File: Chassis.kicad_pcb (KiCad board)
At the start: 2 copper layers, 10 parts, among them J1 Conn_01x02, J10 Conn_01x02, J2 Conn_01x02, J3 Conn_01x02, J4 Conn_01x02, J5 Conn_01x02, J6 Conn_01x02, J7 Conn_01x02, J8 Conn_01x02, J9 Conn_01x02

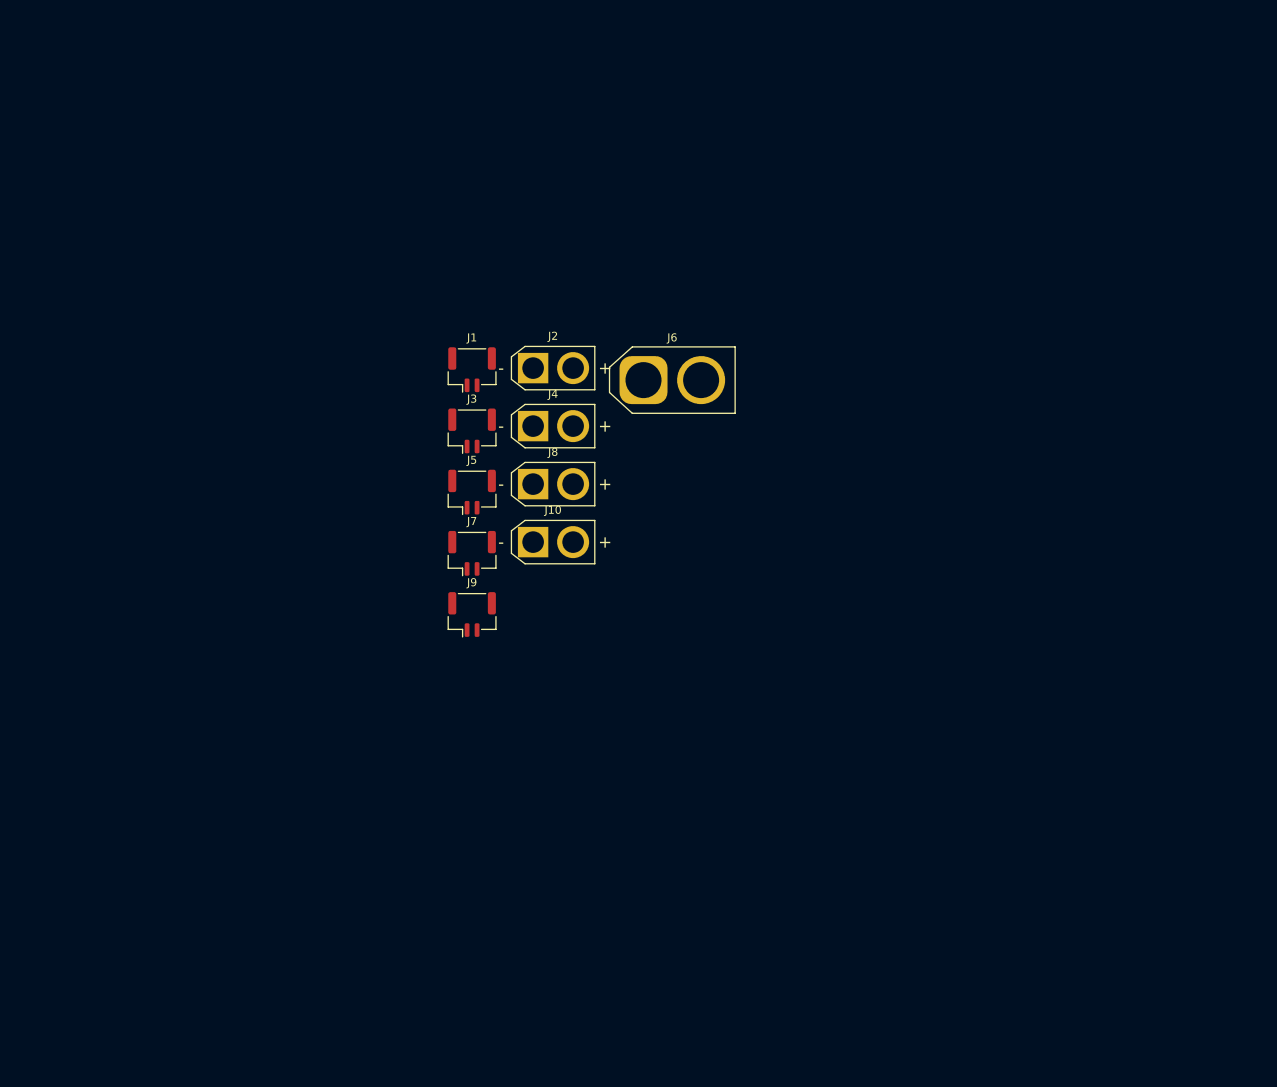
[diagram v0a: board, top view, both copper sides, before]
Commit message: Change polarity of pins + add circular trace
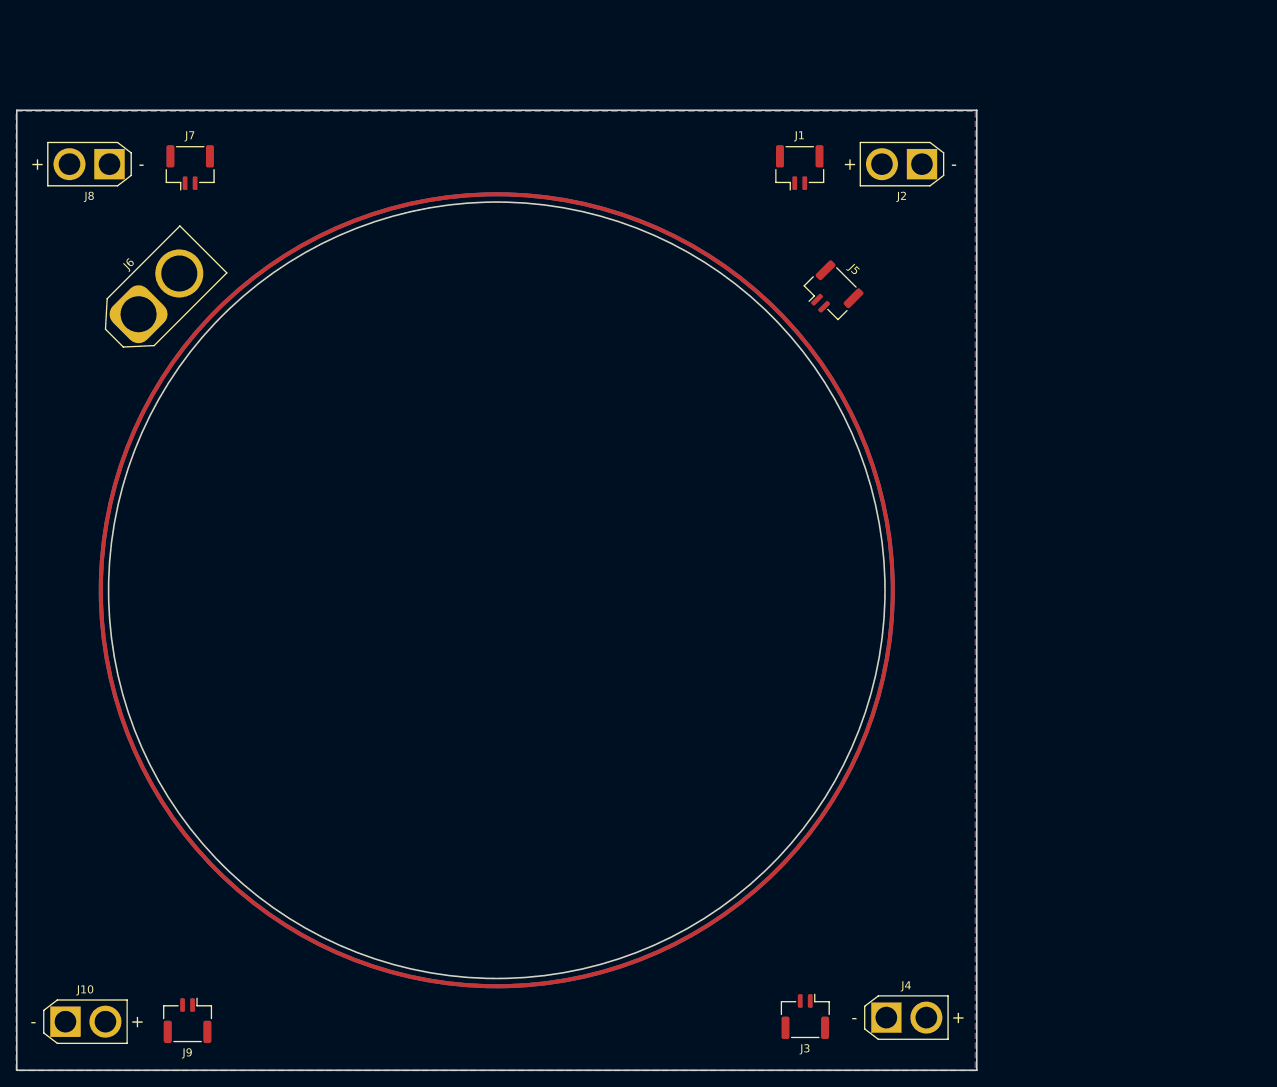
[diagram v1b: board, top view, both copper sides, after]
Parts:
- moved J4 86.1 mm to (168.7, 153.4)
- moved J3 84.2 mm to (158.6, 153.3), turned to 180 degrees
- moved J10 83.7 mm to (66.1, 153.9)
- moved J8 66.4 mm to (71.6, 46.7), turned to 180 degrees
- moved J6 63.7 mm to (75.2, 65.5), turned to 45 degrees
- moved J9 62.0 mm to (81.3, 153.8), turned to 180 degrees
- moved J7 59.7 mm to (81.7, 47.2)
- moved J2 54.9 mm to (173.1, 46.7), turned to 180 degrees
- moved J5 51.4 mm to (161.9, 62.7), turned to -45 degrees
- moved J1 48.1 mm to (157.9, 47.2)
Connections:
- J1 pad 1: /CAN+ -> /CAN-
- J1 pad 2: /CAN- -> /CAN+
- J10 pad 1: /VIN -> /GND
- J10 pad 2: /GND -> /VIN
- J2 pad 1: /VIN -> /GND
- J2 pad 2: /GND -> /VIN
- J3 pad 1: /CAN+ -> /CAN-
- J3 pad 2: /CAN- -> /CAN+
- J4 pad 1: /VIN -> /GND
- J4 pad 2: /GND -> /VIN
- J5 pad 1: /CAN+ -> /CAN-
- J5 pad 2: /CAN- -> /CAN+
- J6 pad 1: /VIN -> /GND
- J6 pad 2: /GND -> /VIN
- J7 pad 1: /CAN+ -> /CAN-
- J7 pad 2: /CAN- -> /CAN+
- J8 pad 1: /VIN -> /GND
- J8 pad 2: /GND -> /VIN
- J9 pad 1: /CAN+ -> /CAN-
- J9 pad 2: /CAN- -> /CAN+
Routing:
- added copper zone on B.Cu, net /GND
- added copper zone on F.Cu, net /VIN
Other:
- board outline added: 120 x 120 mm

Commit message: Routed CAN lines + made hole octagonal
+ differential pair skew fixed
Dimensions may be subject to change, will have to redimension and reroute
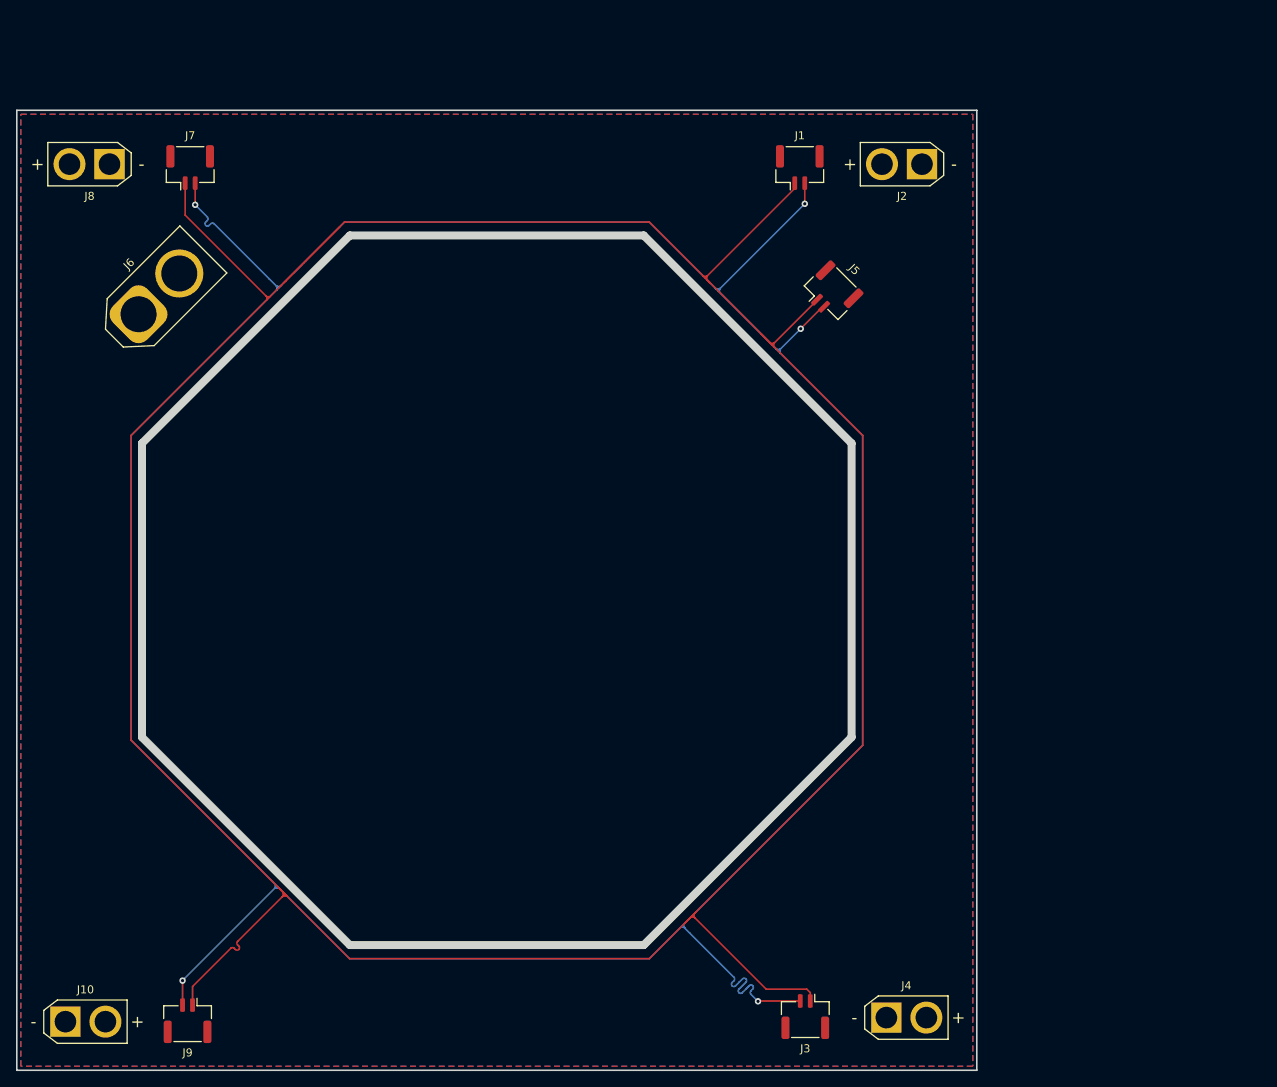
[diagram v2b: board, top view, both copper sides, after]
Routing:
- net /CAN+: track 0.00 -> 417.9 mm, vias 0 -> 5
- net /CAN-: track 0.00 -> 407.2 mm
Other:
- outline, holes or cut-outs redrawn

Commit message: Fixed colinear traces
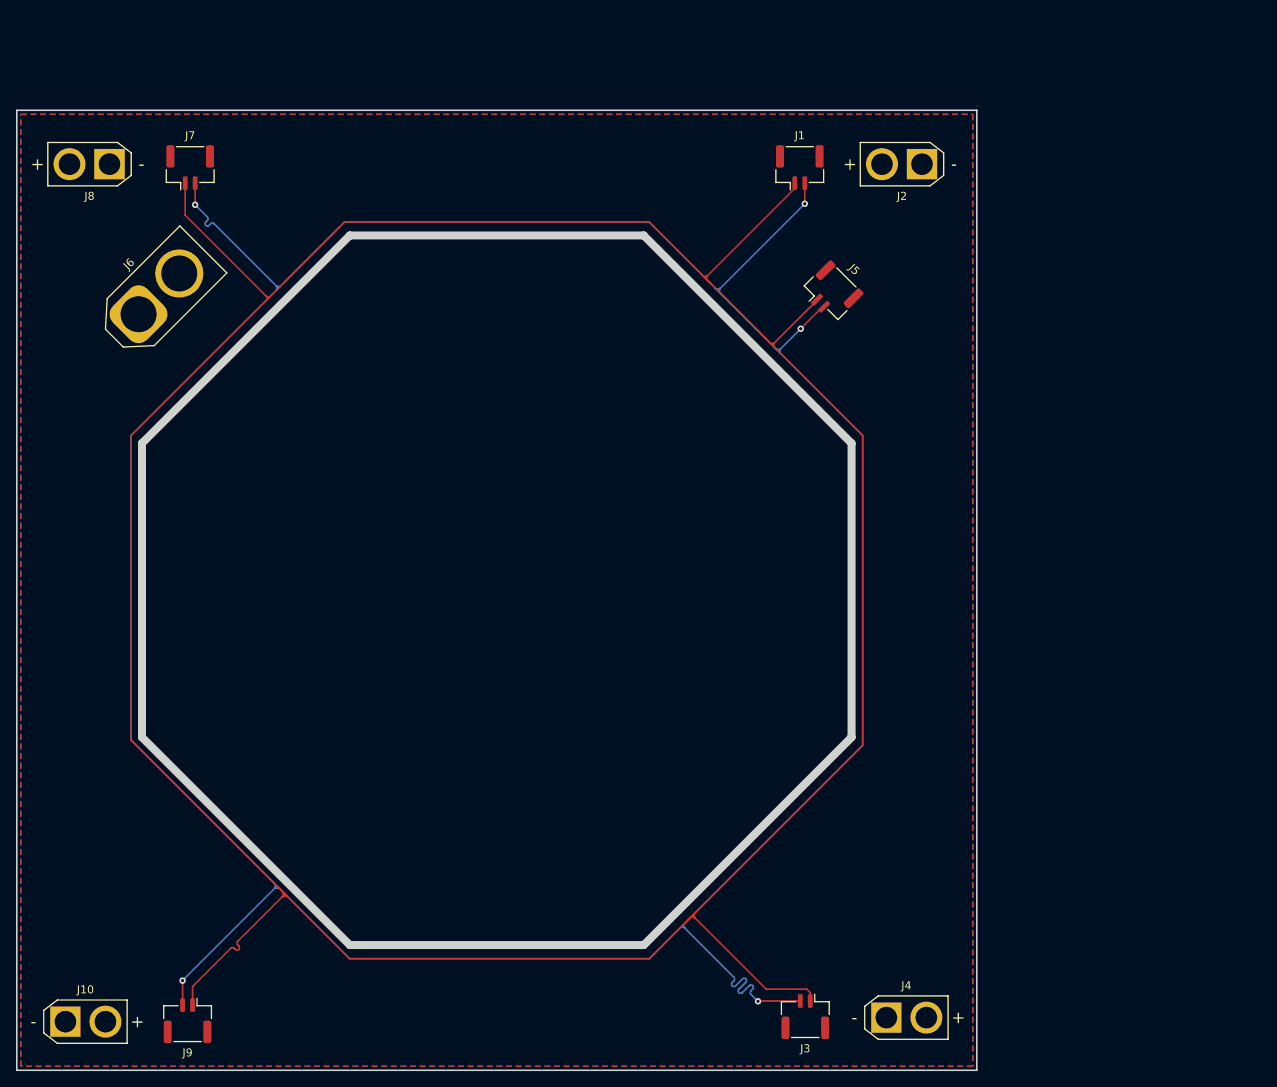
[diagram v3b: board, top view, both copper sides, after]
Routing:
- net /CAN+: track 417.9 -> 416.3 mm
- net /CAN-: track 407.2 -> 406.5 mm

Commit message: Completed initial layout
I'm going to get roasted over some of these choices
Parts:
- added C1: 4.7µF, Capacitor_SMD:C_0603_1608Metric_Pad1.08x0.95mm_HandSolder, F.Cu at (176.2, 145.1)
- added C2: 4.7µF, Capacitor_SMD:C_0603_1608Metric_Pad1.08x0.95mm_HandSolder, F.Cu at (176.2, 147.6)
- added C3: 10nF, Capacitor_SMD:C_0603_1608Metric_Pad1.08x0.95mm_HandSolder, F.Cu at (161.5, 141.7)
- added C4: 22µF, Capacitor_SMD:C_0805_2012Metric_Pad1.18x1.45mm_HandSolder, F.Cu at (176.5, 131.6)
- added C5: 22µF, Capacitor_SMD:C_0805_2012Metric_Pad1.18x1.45mm_HandSolder, F.Cu at (176.5, 134.9)
- added C6: 82pF, Capacitor_SMD:C_0603_1608Metric_Pad1.08x0.95mm_HandSolder, F.Cu at (163.5, 145.0)
- added D1: B550, Robomaster_ICs:SODFL5336X110N, F.Cu at (176.6, 140.0)
- added D2: BAS321J, Diode_SMD:D_SOD-323F, F.Cu at (164.1, 141.7)
- added D3: 150060BS75000, LED_SMD:LED_0603_1608Metric_Pad1.05x0.95mm_HandSolder, F.Cu at (171.2, 130.0)
- added D4: 150060RS75000, LED_SMD:LED_0603_1608Metric_Pad1.05x0.95mm_HandSolder, F.Cu at (71.6, 60.5)
- added IC1: RT6285GSP, Robomaster_ICs:SOIC127P600X175-9N, F.Cu at (169.8, 144.7)
- added L1: 10µH, Robomaster_ICs:MPLAL6060100, F.Cu at (169.9, 137.7)
- added R1: 100kΩ, Resistor_SMD:R_0603_1608Metric_Pad0.98x0.95mm_HandSolder, F.Cu at (163.4, 147.6)
- added R2: 1kΩ, Resistor_SMD:R_0603_1608Metric_Pad0.98x0.95mm_HandSolder, F.Cu at (75.2, 56.9)
- added R3: 6.8kΩ, Resistor_SMD:R_0603_1608Metric_Pad0.98x0.95mm_HandSolder, F.Cu at (167.6, 148.8)
- added R4: 18kΩ, Resistor_SMD:R_0603_1608Metric_Pad0.98x0.95mm_HandSolder, F.Cu at (164.8, 137.5)
- added R5: 4.7kΩ, Resistor_SMD:R_0603_1608Metric_Pad0.98x0.95mm_HandSolder, F.Cu at (162.3, 137.5)
- added R6: 680Ω, Resistor_SMD:R_0603_1608Metric_Pad0.98x0.95mm_HandSolder, F.Cu at (171.2, 132.6)
- added TP1: TestPoint, TestPoint:TestPoint_Pad_1.0x1.0mm, F.Cu at (158.0, 65.0)
- added TP2: TestPoint, TestPoint:TestPoint_Pad_1.0x1.0mm, F.Cu at (159.5, 66.5)
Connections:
- net /GND renamed GND
- net /VIN renamed +24V
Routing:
- net /V_{OUT}: track 0.00 -> 39.2 mm
- net +24V: track 0.00 -> 20.0 mm, vias 0 -> 1
- net /24V -> 19V Buck Convertor/SW: track 0.00 -> 16.9 mm
- net /24V -> 19V Buck Convertor/FB: track 0.00 -> 11.2 mm
- net +5V: track 0.00 -> 8.00 mm
- net /24V -> 19V Buck Convertor/BOOT: track 0.00 -> 5.65 mm
- net Net-(D4-A): track 0.00 -> 3.24 mm
- net Net-(D3-A): track 0.00 -> 2.56 mm
- added copper zone on B.Cu, net +24V
- added copper zone on F.Cu, net /24V -> 19V Buck Convertor/FB
- added copper zone on F.Cu, net /V_{OUT}
- added copper zone on F.Cu, net GND
- removed copper zone on F.Cu, net +24V
- removed copper zone on B.Cu, net GND

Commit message: Finalized board design
I think
Also added more 3D models and whatnot
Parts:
- J10, J2, J4, J8: footprint Connector_AMASS:AMASS_XT30U-F_1x02_P5.0mm_Vertical -> Robomaster_ICs:AMASS_XT30U-F_1x02_P5.0mm_Vertical
- moved C1 30.0 mm to (204.6, 135.3)
- moved C2 30.0 mm to (204.6, 137.8)
- moved C4 30.0 mm to (204.9, 121.8)
- moved D1 30.0 mm to (205.0, 130.3)
- moved D2 30.0 mm to (192.5, 132.0)
- moved D3 30.0 mm to (199.6, 120.3)
- moved J10 30.0 mm to (94.5, 144.2)
- moved J4 30.0 mm to (197.1, 143.7)
- moved J9 30.0 mm to (109.7, 144.1)
- moved L1 30.0 mm to (198.3, 127.9)
- moved R1 30.0 mm to (191.8, 137.8)
- moved R3 30.0 mm to (196.0, 139.1)
- moved R4 30.0 mm to (193.2, 127.8)
- moved C5 30.0 mm to (204.9, 125.1)
- moved J2 30.0 mm to (201.5, 37.0)
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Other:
- outline, holes or cut-outs redrawn

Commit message: Rearrange parts
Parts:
- moved C3 2.87 mm to (192.8, 131.8)
- moved D2 1.97 mm to (190.5, 131.8)
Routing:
- net /24V -> 19V Buck Convertor/SW: track 16.9 -> 13.7 mm
- added copper zone on F.Cu, net +5V
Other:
- board text added: "19V Indicator"
- board text added: "24V IN"
- board text added: "24V Indicator"
- board text added: "CAN Input"
- board text added: "CAN+"
- board text added: "CAN-"
- board text added: "to BL ESC"
- board text added: "to BR ESC"
- board text added: "to FL ESC"
- board text added: "to FR ESC"

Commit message: move around connector
g'night
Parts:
- added J11: Sabre Vertical Header 6, Robomaster_ICs:CON_431602106_MOL, F.Cu at (202.2, 70.4)
- J1: value Conn_01x02 -> FR_JST
- J10: value Conn_01x02 -> BL_XT30
- J2: value Conn_01x02 -> FR_XT30
- J3: value Conn_01x02 -> BR_JST
- J4: value Conn_01x02 -> BR_XT30
- J5: value Conn_01x02 -> IN_JST
- J6: value Conn_01x02 -> IN_XT60
- J7: value Conn_01x02 -> FL_JST
- J8: value Conn_01x02 -> FL_XT30
- J9: value Conn_01x02 -> BL_JST

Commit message: Add power connector
big boy
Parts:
- moved D3 5.84 mm to (205.2, 118.9), turned to -90 degrees
- moved C4 5.83 mm to (200.6, 117.9)
- moved C5 5.82 mm to (200.7, 121.2)
- moved R6 5.77 mm to (205.2, 124.0), turned to 90 degrees
- moved J11 1.66 mm to (203.8, 70.2)
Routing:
- net /V_{OUT}: track 38.7 -> 40.7 mm
- net Net-(D3-A): track 2.56 -> 3.29 mm
- removed copper zone on F.Cu, net /V_{OUT}
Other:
- board size 120 x 120 mm -> 125.5 x 120 mm
